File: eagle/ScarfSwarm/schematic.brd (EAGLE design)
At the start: 100 x 80 mm, 5 parts

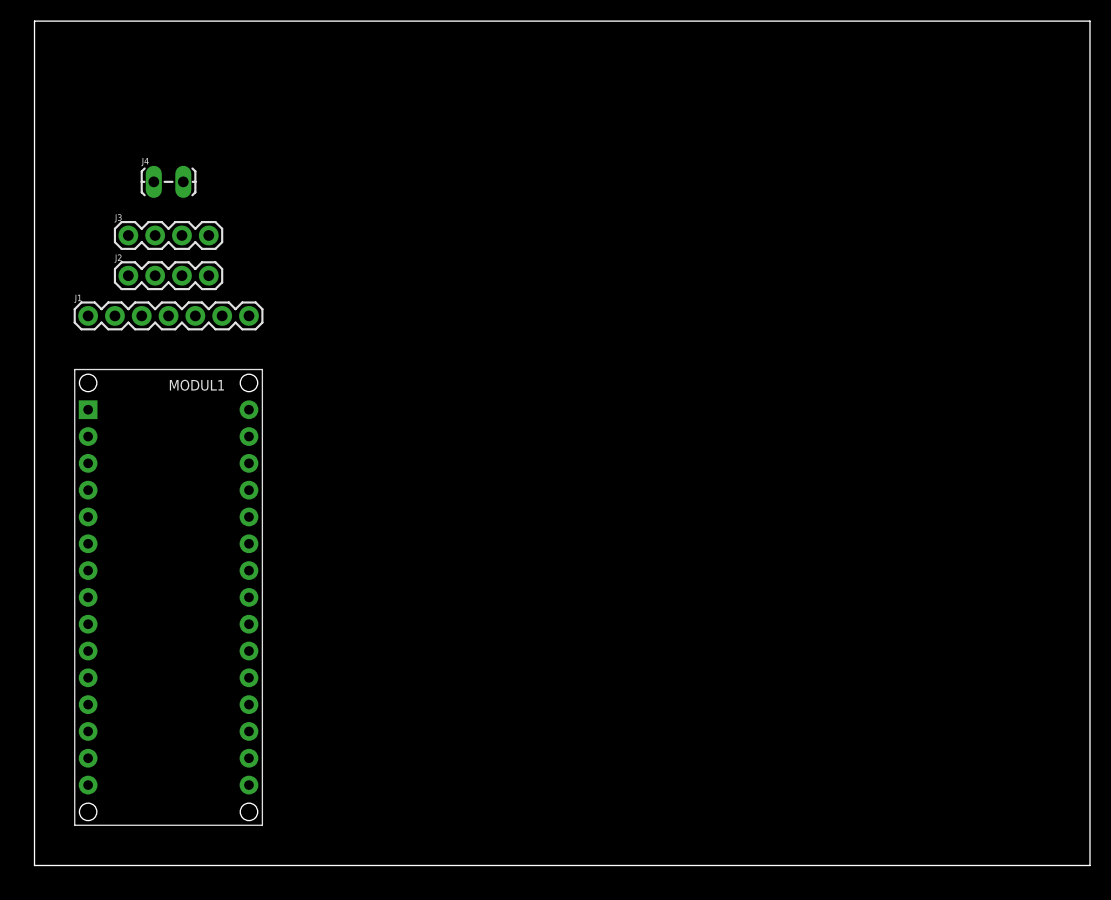
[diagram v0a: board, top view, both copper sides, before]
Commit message: add auto routing with pads on back
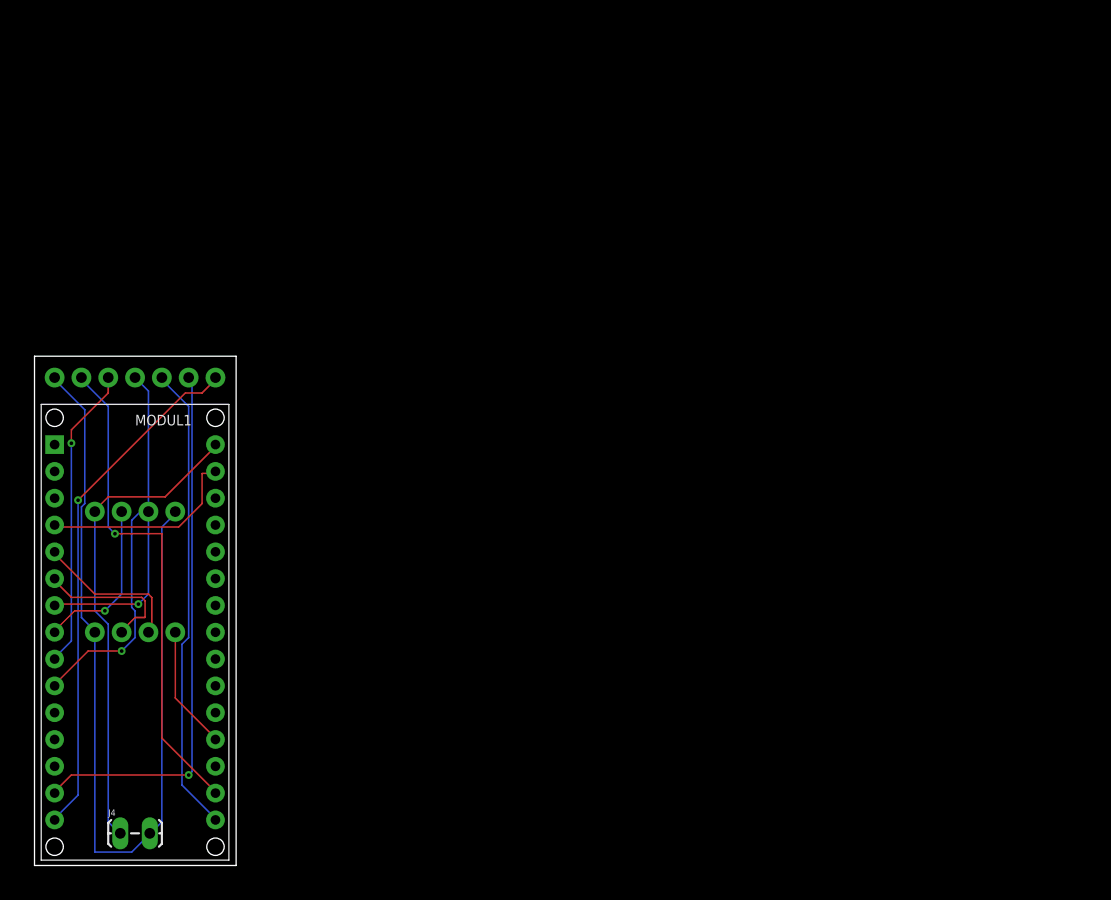
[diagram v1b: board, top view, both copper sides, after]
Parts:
- moved J4 61.8 mm to (8.26, 3.05)
- moved J2 34.1 mm to (13.3, 22.1), flipped to the bottom
- moved J3 26.5 mm to (13.3, 33.5), flipped to the bottom
- moved J1 13.4 mm to (17.1, 46.2), flipped to the bottom
- moved MODUL1 4.58 mm to (9.53, 22.1)
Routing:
- net GND: track 0.00 -> 84.3 mm
- net N$5: track 0.00 -> 51.4 mm, vias 0 -> 1
- net N$6: track 0.00 -> 49.2 mm, vias 0 -> 1
- net N$1: track 0.00 -> 47.2 mm, vias 0 -> 1
- net N$12: track 0.00 -> 45.7 mm
- net N$4: track 0.00 -> 44.5 mm
- net N$3: track 0.00 -> 35.5 mm, vias 0 -> 1
- net N$2: track 0.00 -> 28.8 mm, vias 0 -> 1
- net COM: track 0.00 -> 19.4 mm
- net N$8: track 0.00 -> 17.2 mm, vias 0 -> 1
- net N$13: track 0.00 -> 15.7 mm, vias 0 -> 1
- net N$10: track 0.00 -> 14.7 mm
- net N$9: track 0.00 -> 14.0 mm
- net N$11: track 0.00 -> 11.7 mm
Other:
- board size 100 x 80 mm -> 19.1 x 48.2 mm

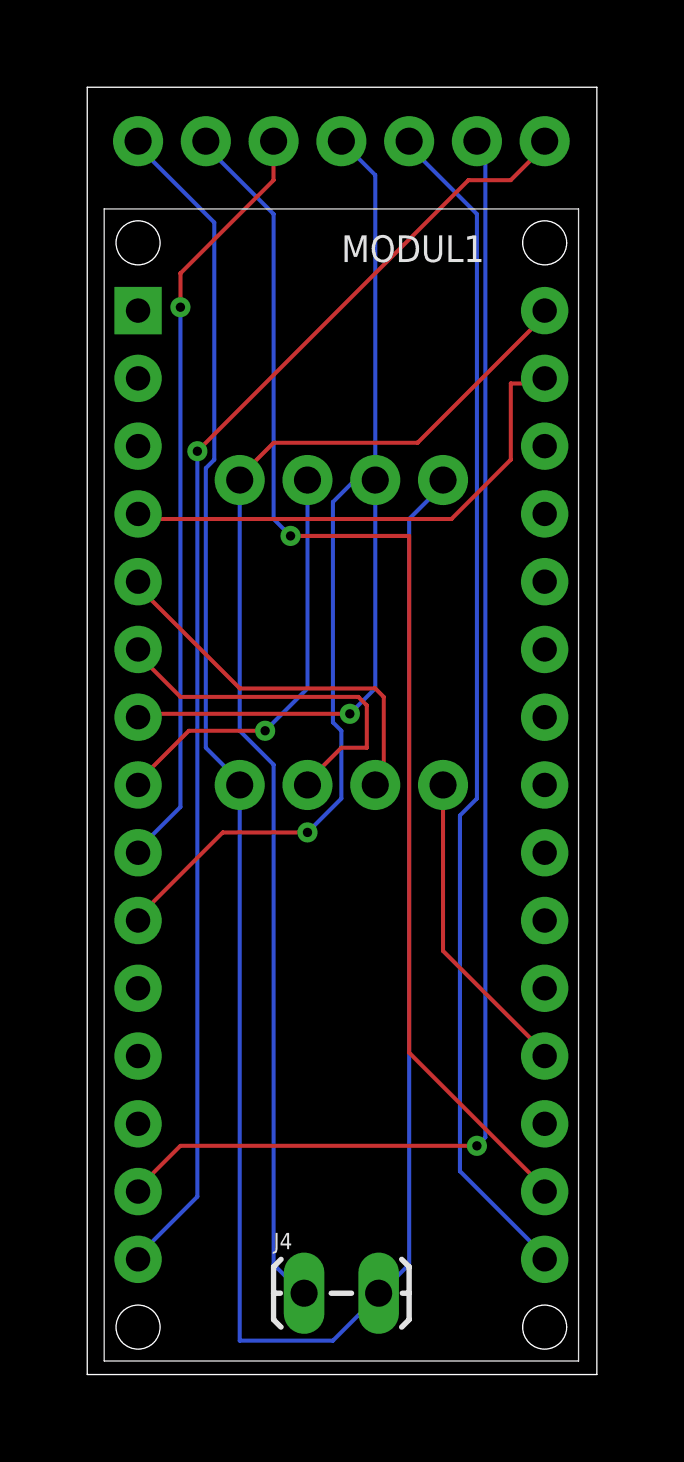
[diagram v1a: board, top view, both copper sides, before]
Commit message: swapped out arduino lib, still have errors
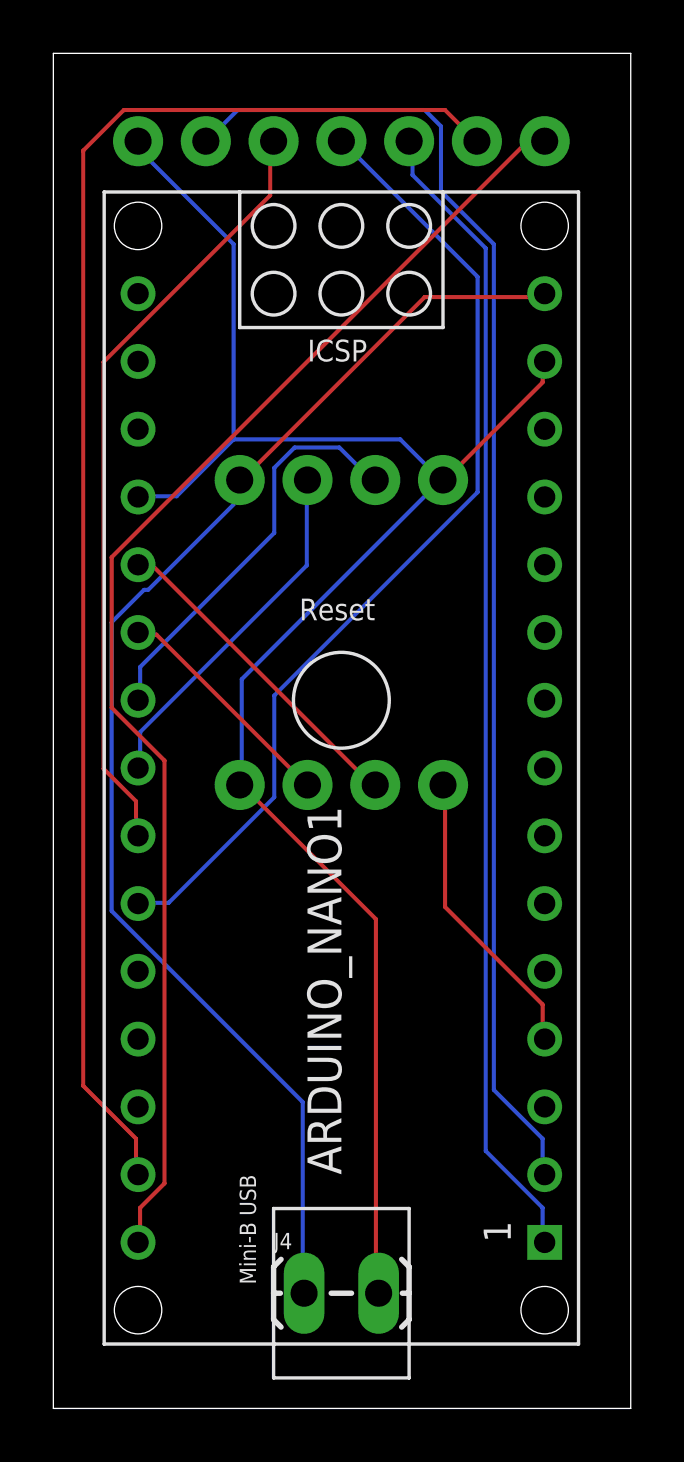
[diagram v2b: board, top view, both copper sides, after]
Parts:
- removed MODUL1: ARDUINO_NANO2, arduino:ARDUINO_NANO2
- added ARDUINO_NANO1: (no value), ArduinoNanoV30:ARDUINO_NANO
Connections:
- removed net +5V: MODUL1.J2.4
- removed net AREF: MODUL1.J2.13
- removed net COM: MODUL1.J1.4, MODUL1.J2.2
- new net 5V: ARDUINO_NANO1.12
- net GND: now also ARDUINO_NANO1.14, ARDUINO_NANO1.19
- net N$1: now also ARDUINO_NANO1.2; no longer MODUL1.J2.14
- net N$10: now also ARDUINO_NANO1.20; no longer MODUL1.J1.5
- net N$11: now also ARDUINO_NANO1.4; no longer MODUL1.J2.12
- net N$12: now also ARDUINO_NANO1.15; no longer MODUL1.J2.1
- net N$13: now also ARDUINO_NANO1.23; no longer MODUL1.J1.8
- net N$2: now also ARDUINO_NANO1.24; no longer MODUL1.J1.9
- net N$3: now also ARDUINO_NANO1.25; no longer MODUL1.J1.10
- net N$4: now also ARDUINO_NANO1.1; no longer MODUL1.J2.15
- net N$5: now also ARDUINO_NANO1.29; no longer MODUL1.J1.14
- net N$6: now also ARDUINO_NANO1.30; no longer MODUL1.J1.15
- net N$8: now also ARDUINO_NANO1.22; no longer MODUL1.J1.7
- net N$9: now also ARDUINO_NANO1.21; no longer MODUL1.J1.6
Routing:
- net COM: track 19.4 -> 0.00 mm
- net GND: track 84.3 -> 67.6 mm
- net N$9: track 14.0 -> 8.72 mm
- net N$12: track 45.7 -> 50.0 mm
- net N$5: track 51.4 -> 55.1 mm, vias 1 -> 0
- net N$1: track 47.2 -> 50.4 mm, vias 1 -> 0
- net N$10: track 14.7 -> 12.3 mm
- net N$13: track 15.7 -> 13.4 mm, vias 1 -> 0
- net N$8: track 17.2 -> 15.5 mm, vias 1 -> 0
- net N$4: track 44.5 -> 43.4 mm
- net N$3: track 35.5 -> 36.6 mm, vias 1 -> 0
- net N$11: track 11.7 -> 11.1 mm
- net N$2: track 28.8 -> 29.2 mm, vias 1 -> 0
- net N$6: track 49.2 -> 49.6 mm, vias 1 -> 0
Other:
- board size 19.1 x 48.2 mm -> 21.6 x 50.8 mm

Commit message: v1 of boards
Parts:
- renumbered J1 to RFCONN, J2 to ROTARY, J3 to LEDSTRIP, J4 to POWER
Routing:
- net N$12: track 50.0 -> 55.2 mm
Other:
- board text added: "13"
- board text added: "3.3V"
- board text added: "Button"
- board text added: "Clock"
- board text added: "D12"
- board text added: "D6"
- board text added: "D7"
- board text added: "Data"
- board text added: "GND"
- board text added: "GND (-)"
- board text added: "Ground"
- board text added: "MOSI/D11"
- board text added: "POS (+)"
- board text added: "Party on Garth."
- board text added: "Party on Wayne."
- board text added: "Rotary A"
- board text added: "Rotary B"
- board text added: "VCC"
- board text added: "v1.0 Jul 29, 2019"

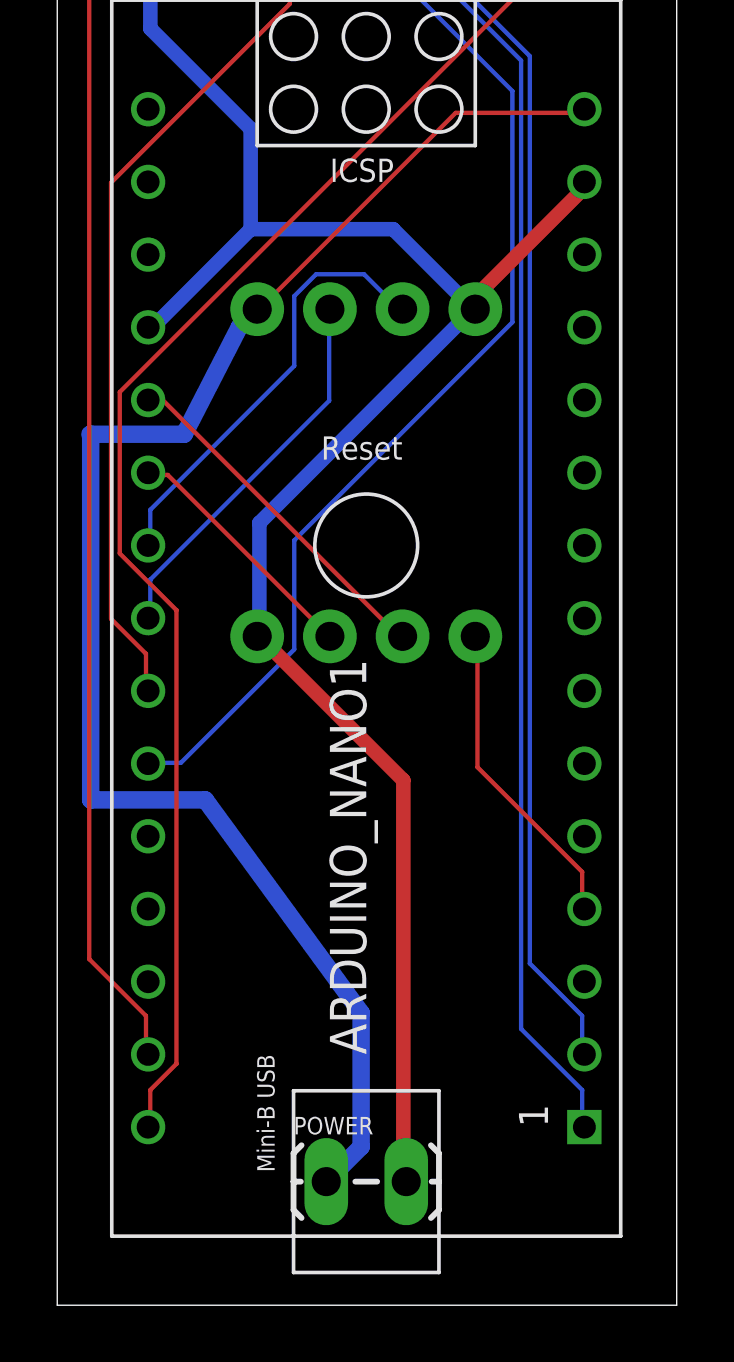
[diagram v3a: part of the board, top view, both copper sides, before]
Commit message: add a little more beef to some of the power lines
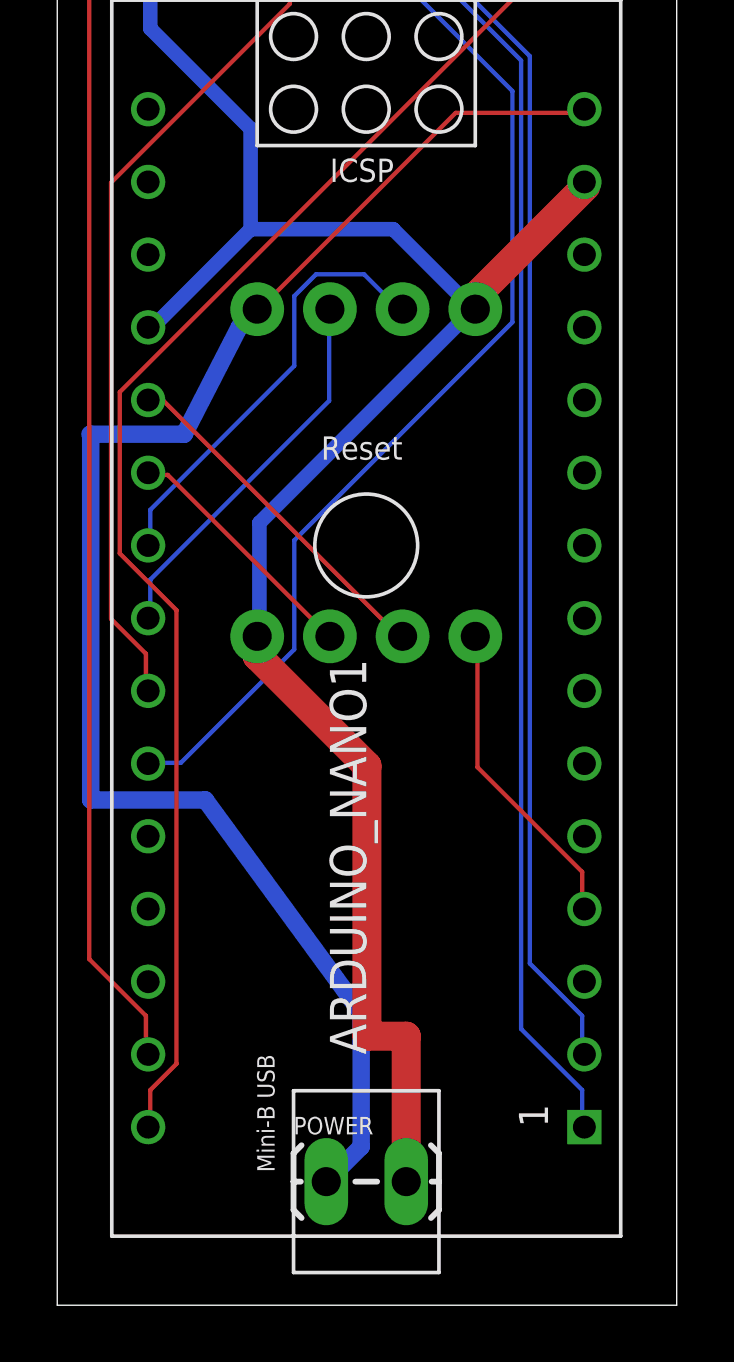
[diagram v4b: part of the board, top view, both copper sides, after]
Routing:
- net GND: track 67.4 -> 68.1 mm
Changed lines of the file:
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@@
 <grid distance="50" unitdist="mil" unit="mil" style="lines" multiple="1" display="yes" altdistance="5" altunitdist="mil" altunit="mil"/>
 <layers>
-<layer number="1" name="Top" color="4" fill="1" visible="no" active="yes"/>
-<layer number="16" name="Bottom" color="1" fill="1" visible="yes" active="yes"/>
+<layer number="1" name="Top" color="4" fill="1" visible="yes" active="yes"/>
+<layer number="16" name="Bottom" color="1" fill="1" visible="no" active="yes"/>
 <layer number="17" name="Pads" color="2" fill="1" visible="yes" active="yes"/>
 <layer number="18" name="Vias" color="2" fill="1" visible="yes" active="yes"/>
 <layer number="19" name="Unrouted" color="6" fill="1" visible="yes" active="yes"/>
 <layer number="20" name="Dimension" color="24" fill="1" visible="yes" active="yes"/>
-<layer number="21" name="tPlace" color="7" fill="1" visible="no" active="yes"/>
-<layer number="22" name="bPlace" color="7" fill="1" visible="yes" active="yes"/>
-<layer number="23" name="tOrigins" color="15" fill="1" visible="no" active="yes"/>
-<layer number="24" name="bOrigins" color="15" fill="1" visible="yes" active="yes"/>
-<layer number="25" name="tNames" color="7" fill="1" visible="no" active="yes"/>
-<layer number="26" name="bNames" color="7" fill="1" visible="yes" active="yes"/>
+<layer number="21" name="tPlace" color="7" fill="1" visible="yes" active="yes"/>
+<layer number="22" name="bPlace" color="7" fill="1" visible="no" active="yes"/>
+<layer number="23" name="tOrigins" color="15" fill="1" visible="yes" active="yes"/>
+<layer number="24" name="bOrigins" color="15" fill="1" visible="no" active="yes"/>
+<layer number="25" name="tNames" color="7" fill="1" visible="yes" active="yes"/>
+<layer number="26" name="bNames" color="7" fill="1" visible="no" active="yes"/>
 <layer number="27" name="tValues" color="7" fill="1" visible="no" active="yes"/>
 <layer number="28" name="bValues" color="7" fill="1" visible="no" active="yes"/>
@@
 <layer number="37" name="tTest" color="7" fill="1" visible="no" active="yes"/>
 <layer number="38" name="bTest" color="7" fill="1" visible="no" active="yes"/>
-<layer number="39" name="tKeepout" color="4" fill="11" visible="no" active="yes"/>
-<layer number="40" name="bKeepout" color="1" fill="11" visible="yes" active="yes"/>
-<layer number="41" name="tRestrict" color="4" fill="10" visible="no" active="yes"/>
-<layer number="42" name="bRestrict" color="1" fill="10" visible="yes" active="yes"/>
+<layer number="39" name="tKeepout" color="4" fill="11" visible="yes" active="yes"/>
+<layer number="40" name="bKeepout" color="1" fill="11" visible="no" active="yes"/>
+<layer number="41" name="tRestrict" color="4" fill="10" visible="yes" active="yes"/>
+<layer number="42" name="bRestrict" color="1" fill="10" visible="no" active="yes"/>
 <layer number="43" name="vRestrict" color="2" fill="10" visible="no" active="yes"/>
 <layer number="44" name="Drills" color="7" fill="1" visible="no" active="yes"/>
@@
 <layer number="49" name="Reference" color="7" fill="1" visible="no" active="yes"/>
 <layer number="50" name="dxf" color="7" fill="1" visible="no" active="no"/>
-<layer number="51" name="tDocu" color="7" fill="1" visible="no" active="yes"/>
-<layer number="52" name="bDocu" color="7" fill="1" visible="yes" active="yes"/>
+<layer number="51" name="tDocu" color="7" fill="1" visible="yes" active="yes"/>
+<layer number="52" name="bDocu" color="7" fill="1" visible="no" active="yes"/>
 <layer number="53" name="tGND_GNDA" color="7" fill="9" visible="no" active="no"/>
 <layer number="54" name="bGND_GNDA" color="1" fill="9" visible="no" active="no"/>
@@
 <contactref element="ROTARY" pad="4"/>
 <contactref element="POWER" pad="2"/>
-<wire x1="10.8204" y1="17.0688" x2="10.8204" y2="3.048" width="0.508" layer="1"/>
-<wire x1="5.7912" y1="22.098" x2="10.8204" y2="17.0688" width="0.508" layer="1"/>
-<wire x1="10.8204" y1="3.048" x2="10.922" y2="3.048" width="0.1524" layer="1"/>
-<wire x1="5.7912" y1="22.098" x2="5.715" y2="22.098" width="0.1524" layer="1"/>
+<wire x1="9.5504" y1="17.5768" x2="9.5504" y2="8.128" width="1.016" layer="1"/>
+<wire x1="9.5504" y1="17.5768" x2="5.715" y2="21.4122" width="1.016" layer="1"/>
+<wire x1="5.715" y1="22.098" x2="5.715" y2="21.4122" width="1.016" layer="1"/>
+<wire x1="10.922" y1="8.128" x2="9.5504" y2="8.128" width="1.016" layer="1"/>
+<wire x1="10.922" y1="8.128" x2="10.922" y2="3.048" width="1.016" layer="1"/>
 <wire x1="2.0828" y1="32.9184" x2="1.9812" y2="32.9184" width="0.1524" layer="16"/>
 <wire x1="5.4864" y1="36.322" x2="2.0828" y2="32.9184" width="0.508" layer="16"/>
@@
 <wire x1="17.145" y1="37.973" x2="17.1958" y2="37.9222" width="0.508" layer="1"/>
 <wire x1="17.1958" y1="37.9222" x2="17.1958" y2="37.8206" width="0.508" layer="1"/>
-<wire x1="17.1958" y1="37.8206" x2="13.335" y2="33.9598" width="0.508" layer="1"/>
+<wire x1="17.1958" y1="37.8206" x2="13.335" y2="33.9598" width="1.016" layer="1"/>
 <wire x1="13.335" y1="33.528" x2="13.335" y2="33.9598" width="0.508" layer="1"/>
 <wire x1="1.9812" y1="43.3324" x2="1.9812" y2="46.1772" width="0.508" layer="16"/>
